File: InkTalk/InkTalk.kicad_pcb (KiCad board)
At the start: 4 copper layers, 60 x 40 mm, 61 parts, among them J1 USB_C_Receptacle_USB2.0_14P, J4 Conn_ARM_SWD_TagConnect_TC2030, U1 Winbond W25Q16JVUXIQ, U2 LM1117, U3 RP2040, U4 SN65HVD1473DGSR, U5 SN65HVD1473DGSR, X1 12MHz

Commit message: InkTalk: Plumb in support for handshake line
I'm unsure if we will _actually_ need this, but this adds in the
option for us to read the handshake status for the printer. One
use for it is getting ThunderScan to work for the ImageWriter which
also uses this line to transfer image data.

Since this is +5v to -5v I've used a little BAT54S diode set with a
big resistor to effectively clamp it to voltage levels safe for the
RP2040. I still need to test this on the prototype units but my napkin
math says it should work.
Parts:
- added C24: 100nF, Capacitor_SMD:C_0402_1005Metric, F.Cu at (129.7, 113.4)
- added D5: BAT54S, Package_TO_SOT_SMD:SOT-23, F.Cu at (140.3, 128.4)
- added R21: 100K, Resistor_SMD:R_0402_1005Metric, F.Cu at (140.8, 125.4)
- moved C15 0.30 mm to (130.8, 113.4)
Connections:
- U3 pad 37: unconnected-(U3-GPIO25-Pad37) -> PRINT_HSKO_CLAMPED
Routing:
- net PRINT_HSKO_CLAMPED: track 0.00 -> 15.6 mm, vias 0 -> 2
- net PRINT_DIN2: track 0.00 -> 15.5 mm, vias 0 -> 1
- net +3V3: track 56.4 -> 59.3 mm, vias 16 -> 17
- net GND: track 30.5 -> 31.1 mm, vias 61 -> 63

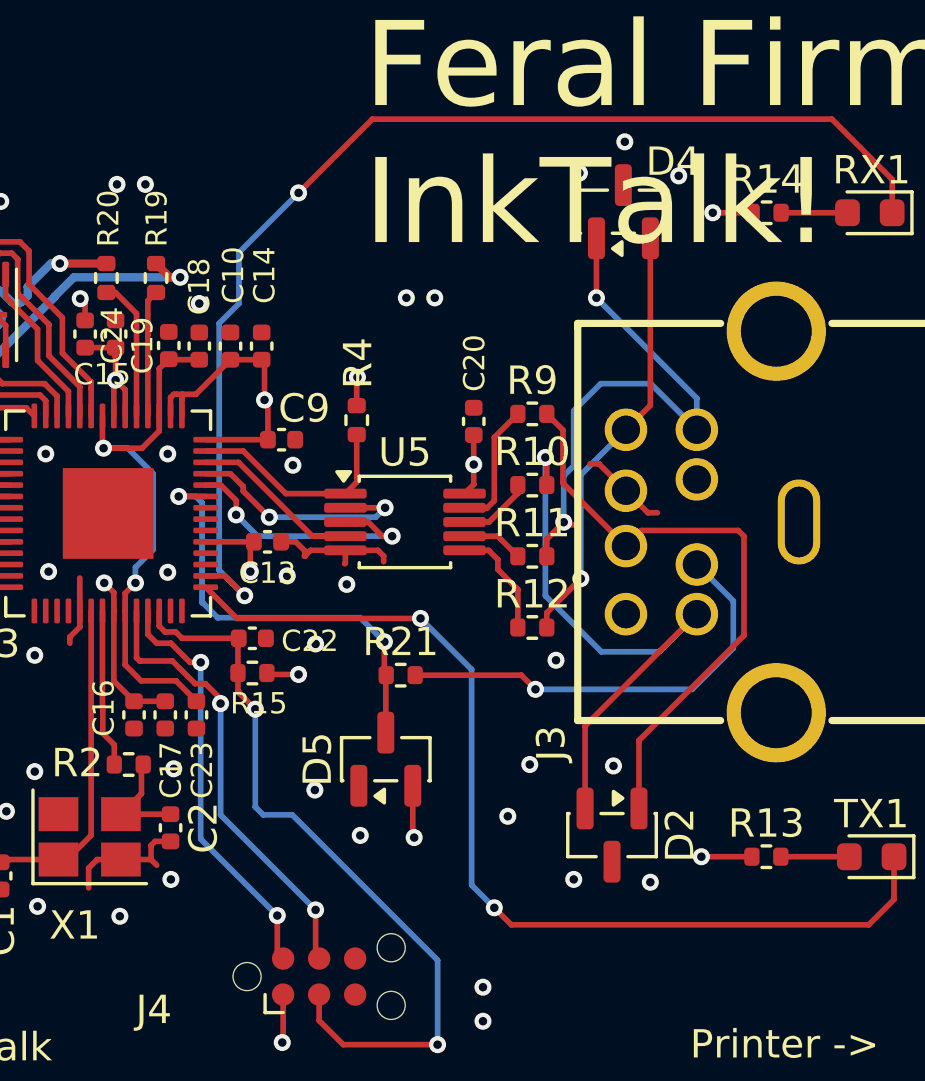
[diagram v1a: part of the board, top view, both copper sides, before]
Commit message: InkTalk: Update board design with issues found
InkTalk is _mostly_ functional out of the box, but I found that the
HSKI/HSKO lines were not as optional as I hoped. On StyleWriters the
printer refused to transmit to us unless we actively drove HSKo, and
on ImageWriters the HSKi line must be actively sampled to avoid
overrunning its buffers.

For HSKo we just tie it up to 3.3v with a 10K pull-up. I cant really see
a case where we will receive very large amounts of data from it and would
need to throttle the printer.

For HSKi I've used a simple diode with a pull down resistor so the -5v
signal for "busy" generates a logic 0 for the RP2040, and when actively
driven to +5v we have a basic resistor divider that drops the voltage
enough to be safe within the IOVDD levels. This is then tied to the UART
hardware flow control pin.

These were verified by me manually patching the wires on the board.
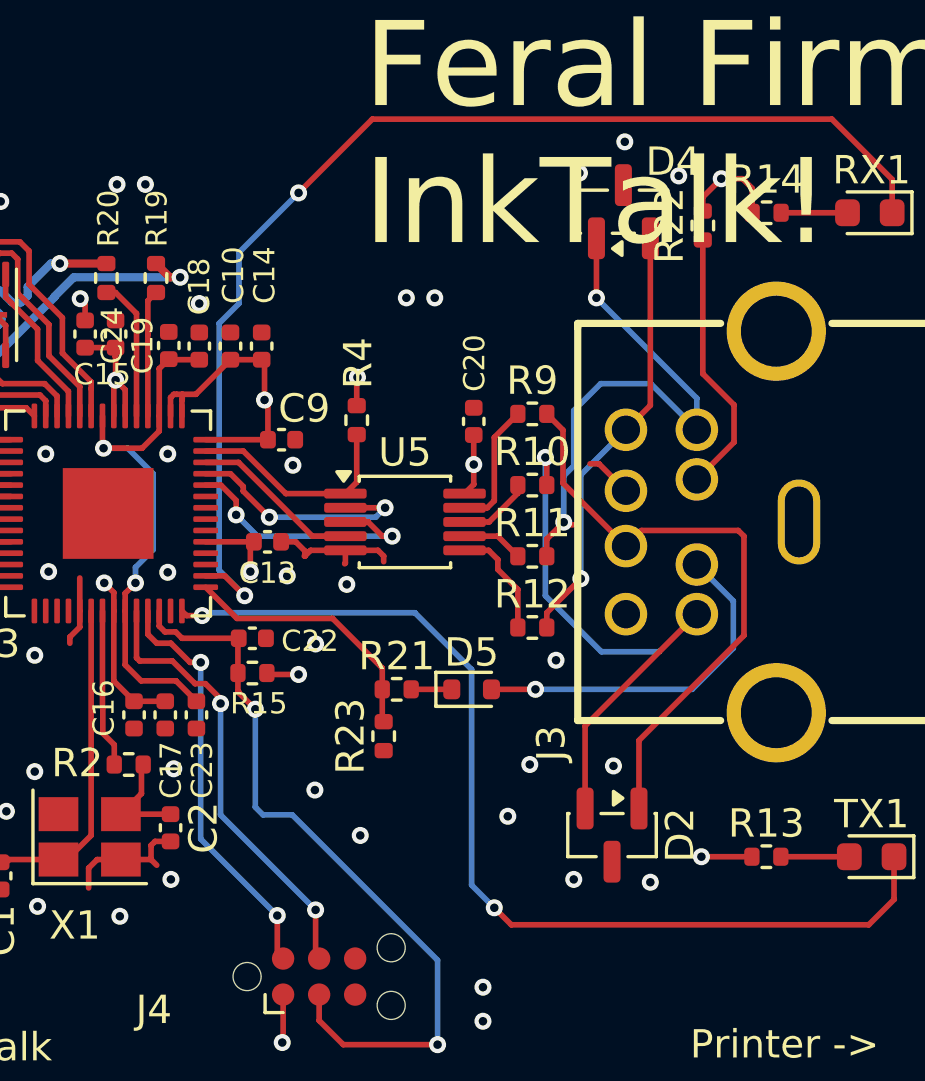
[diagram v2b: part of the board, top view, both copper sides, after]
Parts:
- added R22: 10K, Resistor_SMD:R_0402_1005Metric, F.Cu at (151.4, 109.5)
- added R23: 33K, Resistor_SMD:R_0402_1005Metric, F.Cu at (140.2, 127.5)
- D5: value BAT54S -> 1N4148; footprint Package_TO_SOT_SMD:SOT-23 -> Diode_SMD:D_SOD-523
- R21: value 100K -> 10K
- moved D5 3.90 mm to (143.3, 125.9), turned to 0 degrees
- moved R21 0.52 mm to (140.7, 125.9)
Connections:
- D5 pad 1: GND -> Net-(D5-K)
- D5 pad 2: +3V3 -> PRINT_DIN2
- R21 pad 1: PRINT_HSKO_CLAMPED -> PRINT_HSKI_CLAMPED
- R21 pad 2: PRINT_DIN2 -> Net-(D5-K)
- U1 pad 9: GND -> unconnected-(U1-EP-Pad9)
- U3 pad 28: unconnected-(U3-GPIO17-Pad28) -> Net-(TX1-K)
- U3 pad 29: Net-(TX1-K) -> PRINT_HSKI_CLAMPED
- U3 pad 37: PRINT_HSKO_CLAMPED -> unconnected-(U3-GPIO25-Pad37)
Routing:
- net PRINT_HSKO_CLAMPED: track 15.6 -> 0.00 mm, vias 2 -> 0
- net PRINT_DIN1: track 0.00 -> 9.44 mm
- net PRINT_HSKI_CLAMPED: track 0.00 -> 9.32 mm
- net PRINT_DIN2: track 15.5 -> 12.6 mm
- net GND: track 31.1 -> 29.7 mm
- net Net-(D5-K): track 0.00 -> 1.43 mm
- net Net-(TX1-K): track 35.5 -> 36.1 mm
- net +3V3: track 59.3 -> 59.5 mm, vias 17 -> 16

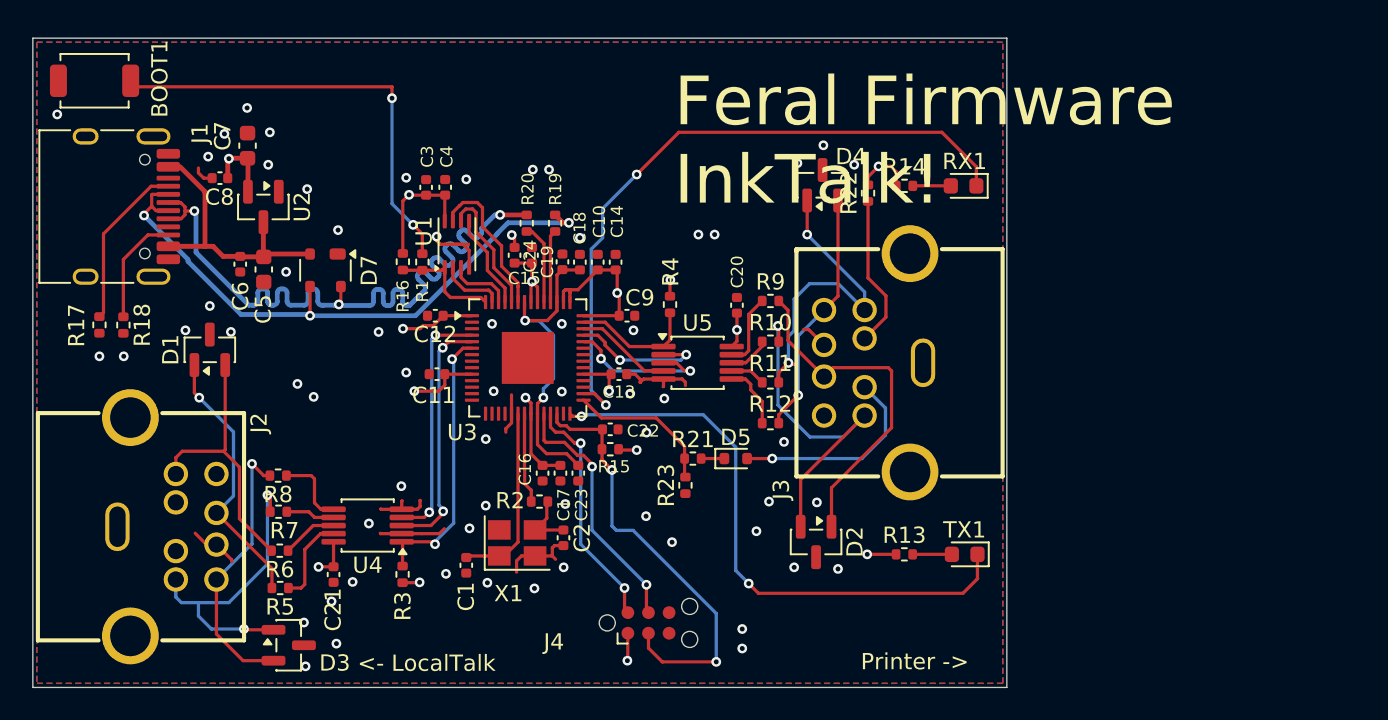
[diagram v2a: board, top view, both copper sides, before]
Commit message: Fix InkTalk and TashTalk USB flipped DIN pins
I accidentally transposed DIN7 and DIN8 when wiring up the connector
in KiCAD (yay weird pin choices on connectors). This explains the rather
odd and unexplainable cases of TashTalk USB not liking resistor pins
on PhoneNET connectors and long cables. It additionally caused InkTalk
to not work at all with the Colour StyleWriter 2200.

Easy fix thankfullly - commit contains just that flip around and some
minor board clean up for the first production-ish run of InkTalk.
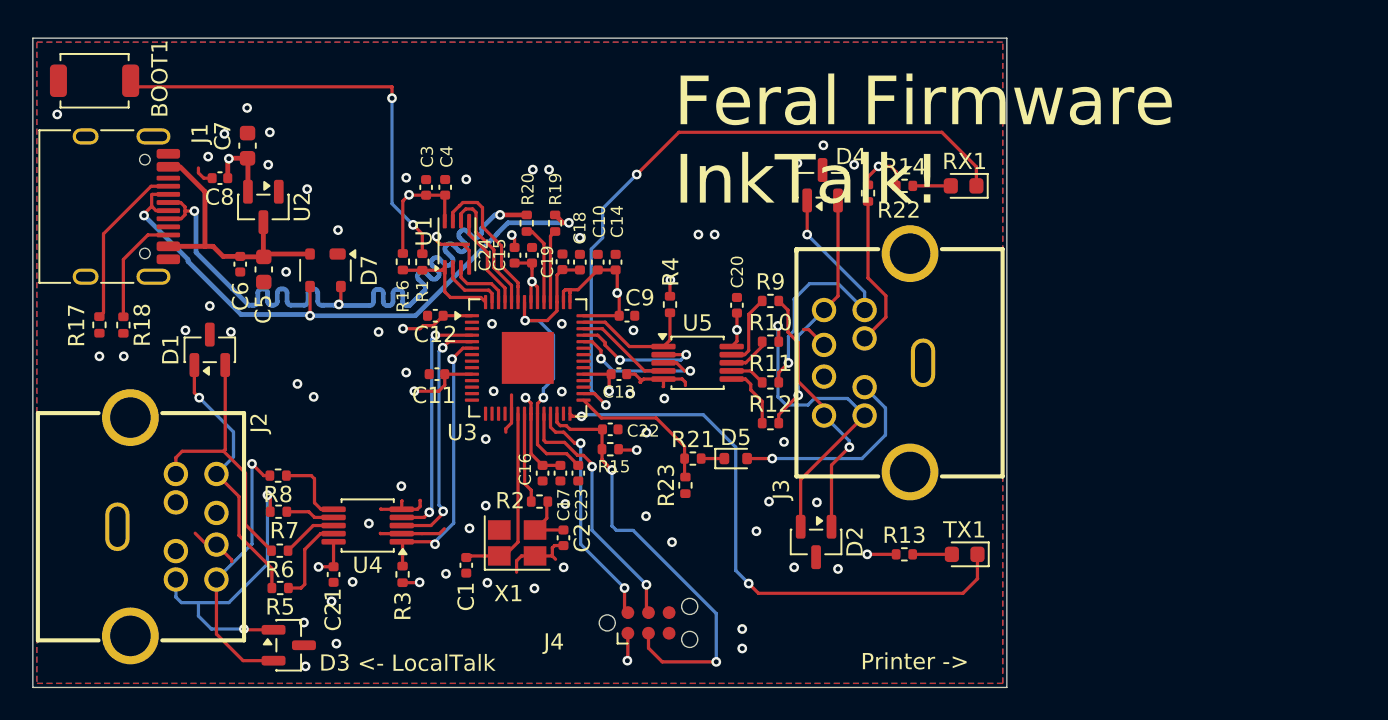
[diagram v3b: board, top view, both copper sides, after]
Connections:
- J2 pad 6: DIN7 -> A
- J2 pad 7: A -> DIN7
- J3 pad 6: PRINT_DIN7 -> PRINT_A
- J3 pad 7: PRINT_A -> PRINT_DIN7
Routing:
- net PRINT_A: track 21.9 -> 16.2 mm, vias 0 -> 1
- net PRINT_B: track 21.1 -> 20.0 mm

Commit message: InkTalk: Production ready tweaks
Handful of last changes I did before I sent the order off for production
yesterday. I changed the 10K / 33K combo for HSKi to 1K / 3K3 so we
could potentially use it for external clock mode, and then a few parts
updates like changing to Microchip's 3V3 reg, and assigning the right
LCSC part for D5.
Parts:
- R21: value 10K -> 1K
- R23: value 33K -> 3K3
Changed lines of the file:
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@@
 			)
 		)
+		(property "LCSC" "C7420320"
+			(at 0 0 0)
+			(layer "F.SilkS")
+			(hide yes)
+			(effects
+				(font
+					(size 1.27 1.27)
+					(thickness 0.15)
+				)
+			)
+		)
 		(property ki_fp_filters "D*DO?35*")
 		(sheetname "/")
@@
 			)
 		)
-		(property "Value" "33K"
+		(property "Value" "3K3"
 			(at 0 1.17 90)
 			(layer "F.Fab")
@@
 			)
 		)
-		(property "LCSC" "C25804 "
+		(property "LCSC" "C25890"
 			(at 0 0 90)
 			(unlocked yes)
@@
 			)
 		)
-		(property "Value" "10K"
+		(property "Value" "1K"
 			(at 0 1.17 0)
 			(layer "F.Fab")
@@
 				)
 			)
+		)
+		(property "LCSC" "C33844"
+			(at 0 0 0)
+			(layer "F.SilkS")
+			(hide yes)
+			(effects
+				(font
+					(size 1.27 1.27)
+					(thickness 0.15)
+				)
+			)
